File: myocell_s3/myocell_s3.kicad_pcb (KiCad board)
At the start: 4 copper layers, 100 parts, among them J1 Conn_01x08, J5 Battery Connector JC2, J7 USB_C_Receptacle_USB2.0_16P, Q3 DMG3404L, SW1 SW_Push, SW2 SW_Push, U1 MSS22D18, U2 ADS1298xPAG, U4 ESP32-S3-WROOM-2, U6 AP2112K-3.3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

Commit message: working on parts placement
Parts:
- R25: value 1k -> 2k
- moved C37 11.7 mm to (163.5, 88.5), turned to 180 degrees
- moved C24 10.7 mm to (170.0, 61.5), turned to 0 degrees
- moved R15 10.5 mm to (160.5, 63.0), turned to -90 degrees
- moved C35 10.3 mm to (163.5, 80.5), turned to 0 degrees
- moved U7 9.24 mm to (163.6, 84.5), turned to 90 degrees
- moved J5 8.25 mm to (150.7, 91.0)
- moved U1 8.14 mm to (151.0, 106.0), turned to 90 degrees
- moved C40 8.02 mm to (160.0, 100.0), turned to 0 degrees
- moved SW1 7.60 mm to (158.0, 55.2), turned to 180 degrees
- moved R26 7.52 mm to (157.5, 81.5), turned to -90 degrees
- moved R14 7.00 mm to (160.5, 72.5), turned to 90 degrees
- moved J1 6.02 mm to (161.5, 118.5)
- moved D7 5.83 mm to (163.5, 96.0), turned to 90 degrees
- moved Q3 5.57 mm to (160.0, 96.4)
- moved C55 5.09 mm to (165.5, 70.0)
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
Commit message: working on components placement
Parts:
- moved C34 52.8 mm to (159.5, 83.0)
- moved C36 52.8 mm to (168.5, 83.0)
- moved U6 52.8 mm to (163.9, 82.9)
- moved C39 23.6 mm to (197.8, 73.5)
- moved R32 19.1 mm to (197.5, 52.5), turned to 180 degrees
- moved D8 16.5 mm to (202.5, 52.5)
- moved U8 15.8 mm to (201.0, 73.6), turned to 90 degrees
- moved J4 15.0 mm to (190.0, 83.5)
- moved J2 14.6 mm to (169.9, 83.5)
- moved J5 14.4 mm to (158.7, 103.0)
- moved C57 13.9 mm to (187.0, 75.0), turned to 90 degrees
- moved J3 13.0 mm to (169.9, 98.4)
- moved C38 13.0 mm to (201.0, 77.5), turned to 180 degrees
- moved C40 12.9 mm to (167.5, 110.5)
- moved D7 12.9 mm to (171.0, 106.5)
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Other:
- board outline added: 52 x 71 mm

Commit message: working on components placement
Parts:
- moved J1 32.4 mm to (200.6, 106.3), turned to 90 degrees
- moved D7 26.5 mm to (159.8, 82.5), turned to 180 degrees
- moved C40 24.8 mm to (163.8, 86.0), turned to 90 degrees
- moved Q3 22.2 mm to (160.2, 86.0), turned to 0 degrees
- moved R27 20.4 mm to (156.2, 86.0), turned to 90 degrees
- moved C34 11.9 mm to (170.0, 88.5), turned to 180 degrees
- moved R26 9.26 mm to (163.5, 99.8), turned to 0 degrees
- moved U1 8.59 mm to (167.0, 115.8), turned to 0 degrees
- moved C35 7.77 mm to (162.5, 93.8), turned to 90 degrees
- moved R25 7.04 mm to (163.5, 97.2), turned to 0 degrees
- moved U6 6.32 mm to (169.9, 84.6), turned to 90 degrees
- moved C21 6.16 mm to (174.5, 112.8)
- moved R2 5.67 mm to (174.5, 110.0)
- moved C2 4.85 mm to (194.2, 108.5)
- moved C28 4.85 mm to (184.5, 108.5)
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
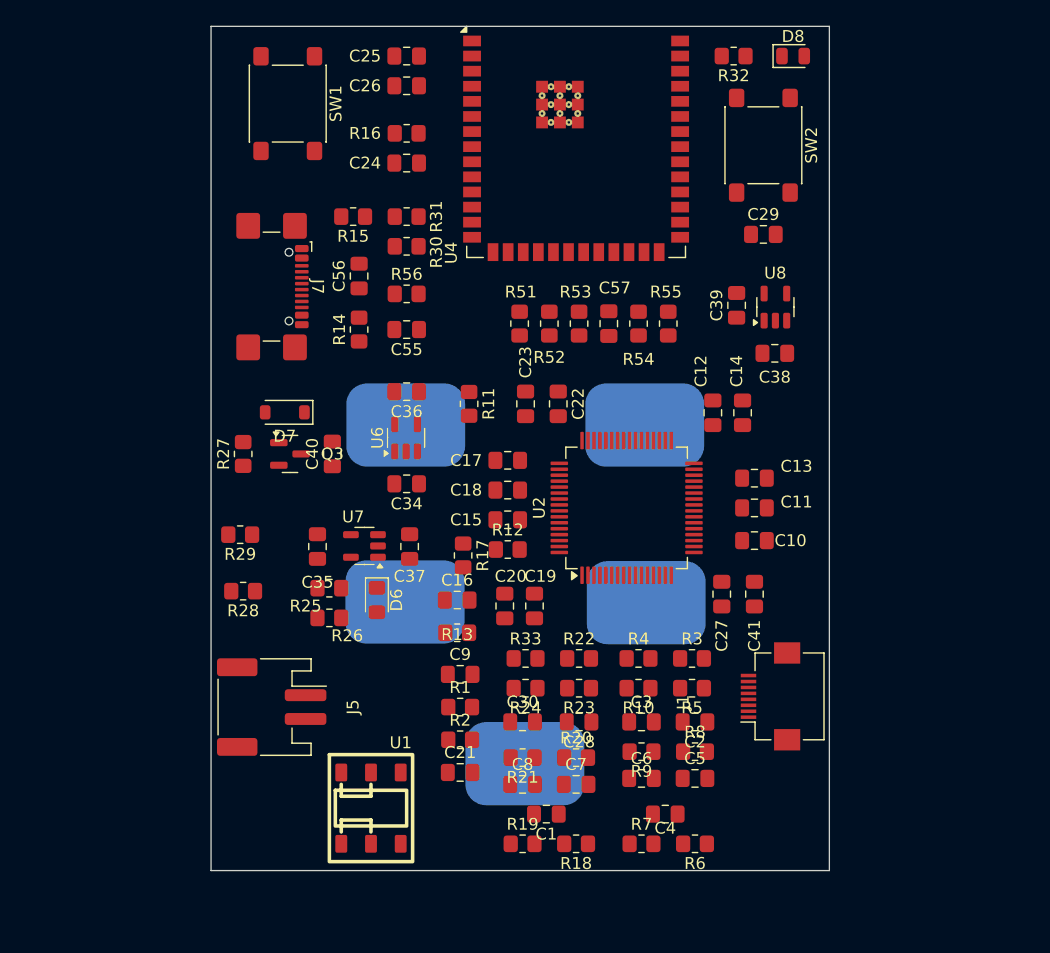
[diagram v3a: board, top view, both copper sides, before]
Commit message: schematic updated: channels 3,4 is onboard now
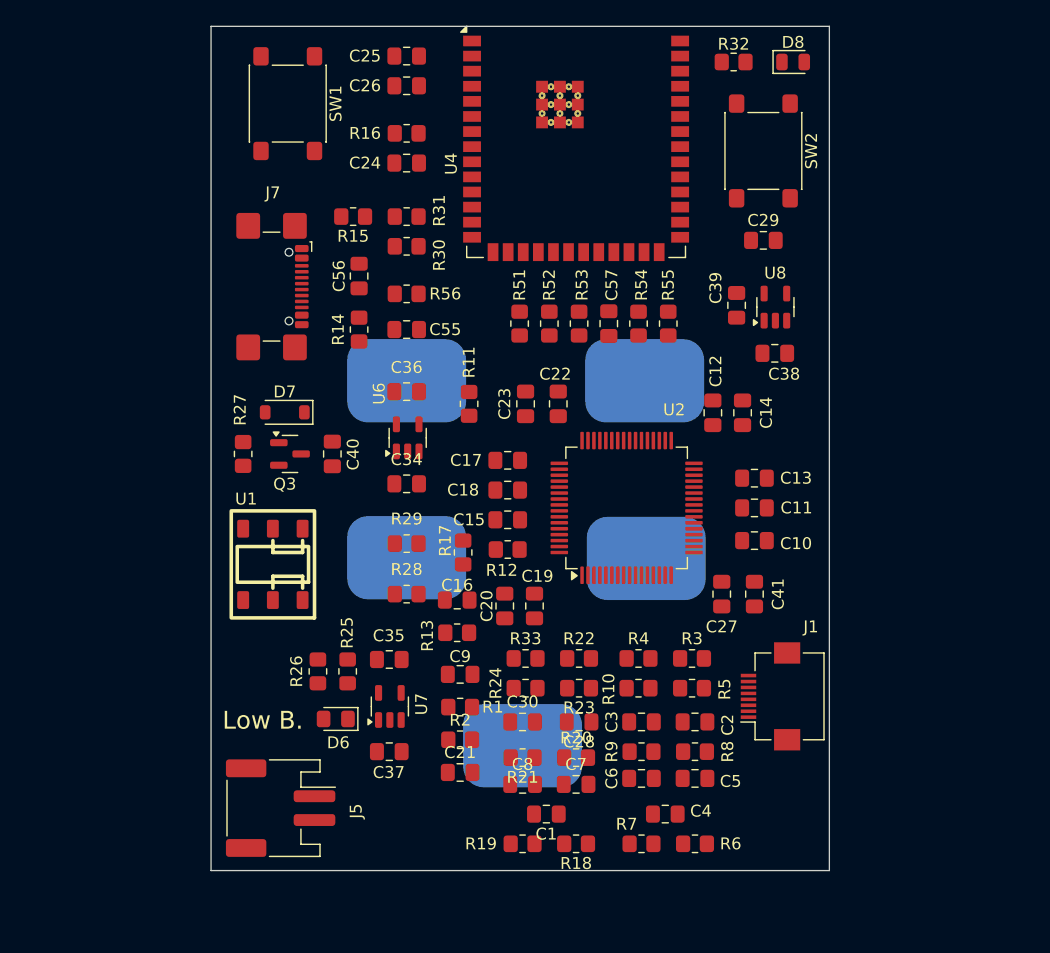
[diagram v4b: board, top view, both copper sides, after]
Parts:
- J2: value ~ -> IN3P
- J3: value ~ -> IN3N
- J4: value ~ -> IN4P
- J6: value ~ -> IN4N
- J8: value ~ -> RLD
- moved U1 22.1 mm to (158.8, 95.2), turned to 180 degrees
- moved C37 17.3 mm to (168.5, 111.0), turned to 180 degrees
- moved R29 14.0 mm to (170.0, 93.5)
- moved R28 13.8 mm to (170.0, 97.8)
- moved U7 13.7 mm to (168.6, 107.2), turned to 90 degrees
- moved C35 11.3 mm to (168.5, 103.2), turned to 0 degrees
- moved D6 10.6 mm to (164.0, 108.2), turned to 180 degrees
- moved J5 8.53 mm to (159.4, 115.8)
- moved R25 7.17 mm to (165.0, 104.2), turned to -90 degrees
- moved R26 4.60 mm to (162.5, 104.2), turned to -90 degrees
- moved J3 3.72 mm to (170.0, 94.7)
- moved J2 3.72 mm to (170.0, 79.8)
- moved J4 3.72 mm to (190.0, 79.8)
- moved J6 3.72 mm to (190.2, 94.8)
- moved J8 1.52 mm to (179.8, 110.5)
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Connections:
- net /adc_8/IN1NF renamed /adc_8/IN3NF
- net /adc_8/IN1PF renamed /adc_8/IN3PF
- net /adc_8/IN2NF renamed /adc_8/IN4NF
- net /adc_8/IN2PF renamed /adc_8/IN4PF
- C2 pad 2: Net-(U2-IN1P) -> Net-(U2-IN3P)
- C28 pad 2: Net-(U2-IN2P) -> Net-(U2-IN4P)
- C3 pad 2: Net-(U2-IN1N) -> Net-(U2-IN3N)
- C30 pad 2: Net-(U2-IN2N) -> Net-(U2-IN4N)
- J1 pad 3: /adc_8/IN4N -> /adc_8/IN2N
- J1 pad 4: /adc_8/IN4P -> /adc_8/IN2P
- J1 pad 6: /adc_8/IN3N -> /adc_8/IN1N
- J1 pad 7: /adc_8/IN3P -> /adc_8/IN1P
- R10 pad 1: Net-(U2-IN1N) -> Net-(U2-IN3N)
- R22 pad 1: Net-(U2-IN2P) -> Net-(U2-IN4P)
- R23 pad 2: Net-(U2-IN2P) -> Net-(U2-IN4P)
- R24 pad 1: Net-(U2-IN2N) -> Net-(U2-IN4N)
- R3 pad 1: Net-(U2-IN1P) -> Net-(U2-IN3P)
- R33 pad 2: Net-(U2-IN2N) -> Net-(U2-IN4N)
- R4 pad 2: Net-(U2-IN1N) -> Net-(U2-IN3N)
- R5 pad 2: Net-(U2-IN1P) -> Net-(U2-IN3P)
- U2 pad 10: /adc_8/IN4P -> Net-(U2-IN4P)
- U2 pad 11: /adc_8/IN3N -> Net-(U2-IN3N)
- U2 pad 12: /adc_8/IN3P -> Net-(U2-IN3P)
- U2 pad 13: Net-(U2-IN2N) -> /adc_8/IN2N
- U2 pad 14: Net-(U2-IN2P) -> /adc_8/IN2P
- U2 pad 15: Net-(U2-IN1N) -> /adc_8/IN1N
- U2 pad 16: Net-(U2-IN1P) -> /adc_8/IN1P
- U2 pad 9: /adc_8/IN4N -> Net-(U2-IN4N)
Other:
- board text added: "Low B."

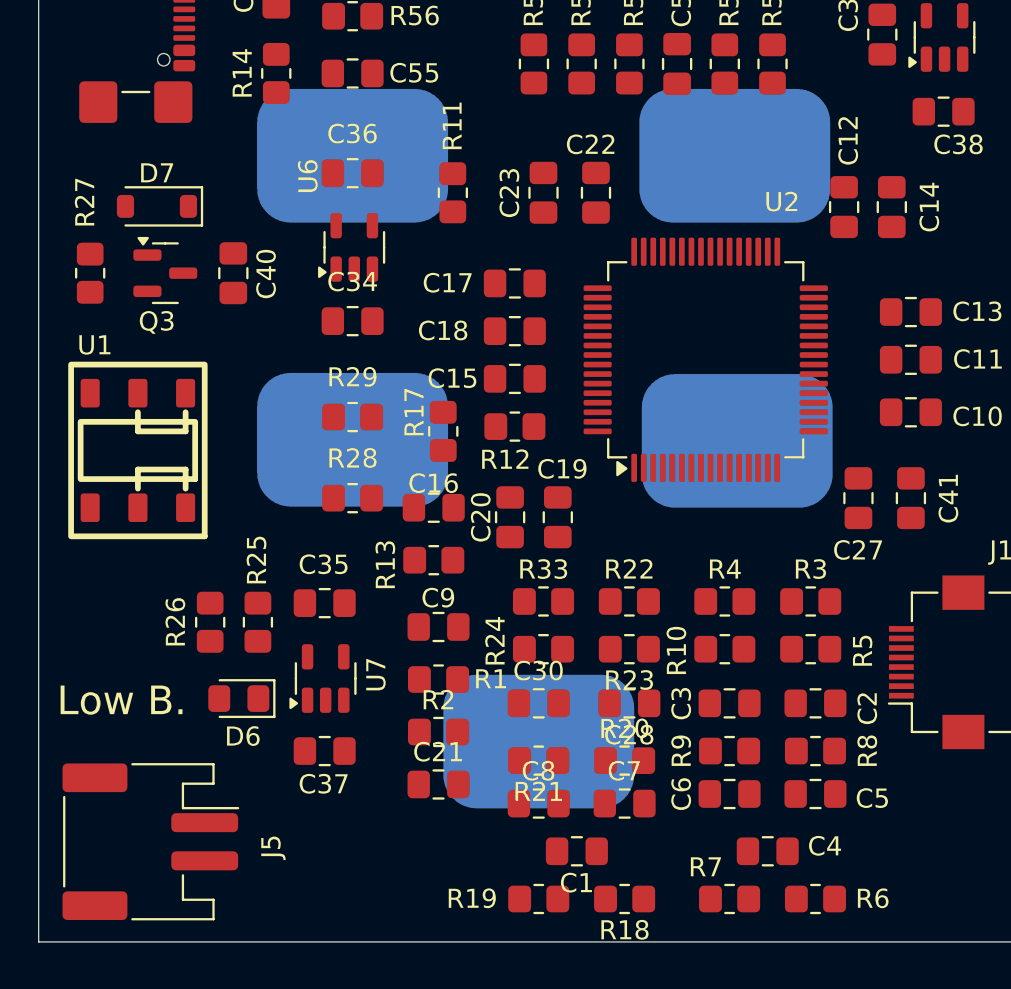
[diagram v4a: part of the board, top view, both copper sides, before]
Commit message: components placement
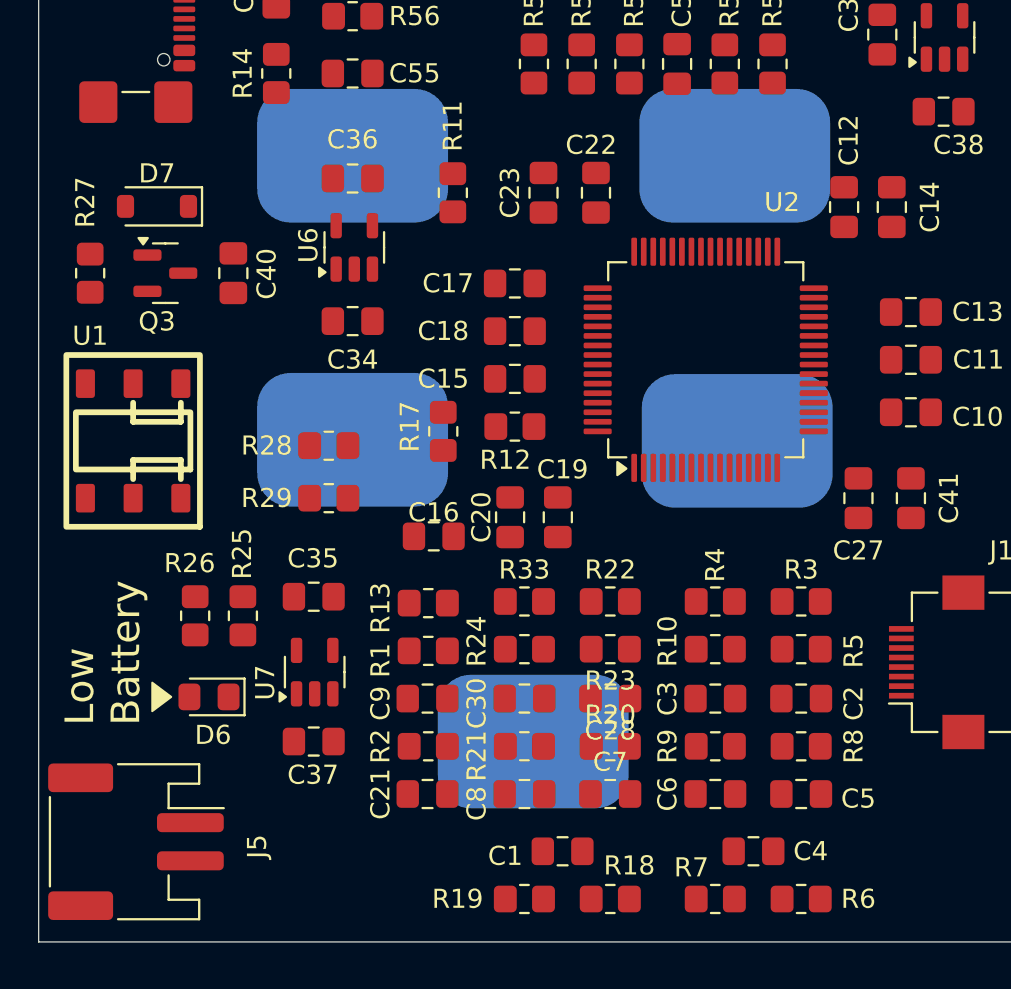
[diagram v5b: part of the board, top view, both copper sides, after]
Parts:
- moved C9 3.79 mm to (173.9, 108.2), turned to 180 degrees
- moved R13 2.27 mm to (174.0, 103.2)
- moved R29 1.95 mm to (168.8, 95.0), turned to 0 degrees
- moved R1 1.59 mm to (174.0, 105.8), turned to 180 degrees
- moved D6 1.56 mm to (162.5, 108.2)
- moved C16 1.50 mm to (174.2, 99.8)
- moved R28 1.25 mm to (168.8, 97.8)
- moved R20 1.06 mm to (183.5, 110.8)
- moved R21 1.06 mm to (179.0, 110.8)
- moved C28 1.03 mm to (183.5, 108.2)
- moved R22 1.00 mm to (183.5, 103.2)
- moved R23 1.00 mm to (183.5, 105.7)
- moved R24 1.00 mm to (179.0, 105.7)
- moved R33 1.00 mm to (179.0, 103.2)
- moved R2 0.92 mm to (174.0, 110.8)
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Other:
- board text added: "Low Battery"
- board text removed: "Low B."
